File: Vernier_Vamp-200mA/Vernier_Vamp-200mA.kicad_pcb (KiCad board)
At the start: 4 copper layers, 160 x 99.5 mm, 209 parts, among them J1 Conn_01x02, J2 RJ45, J3 Screw_Terminal_01x04, J4 Conn_02x07_Odd_Even, J5 Channel 3, J6 Channel 2, J7 Channel 1, Q1 Si4447ADY, Q2 IRF8707PbF, SW1 DPDT_Hirose, U1 LM4040DBZ-5, U10 OPA2277, U11 OPA2277, U12 OPA2277, U13 OPA2277, U14 OPA2277, U15 OPA1622, U16 OPA1622, U17 OPA1622, U2 LM4040DBZ-5, U3 LM393, U4 TPS7A470x, U5 TPS7A470x, U6 TPS7A33, U7 LTC6655-2.5, U8 DAC8814, U9 OPA2277

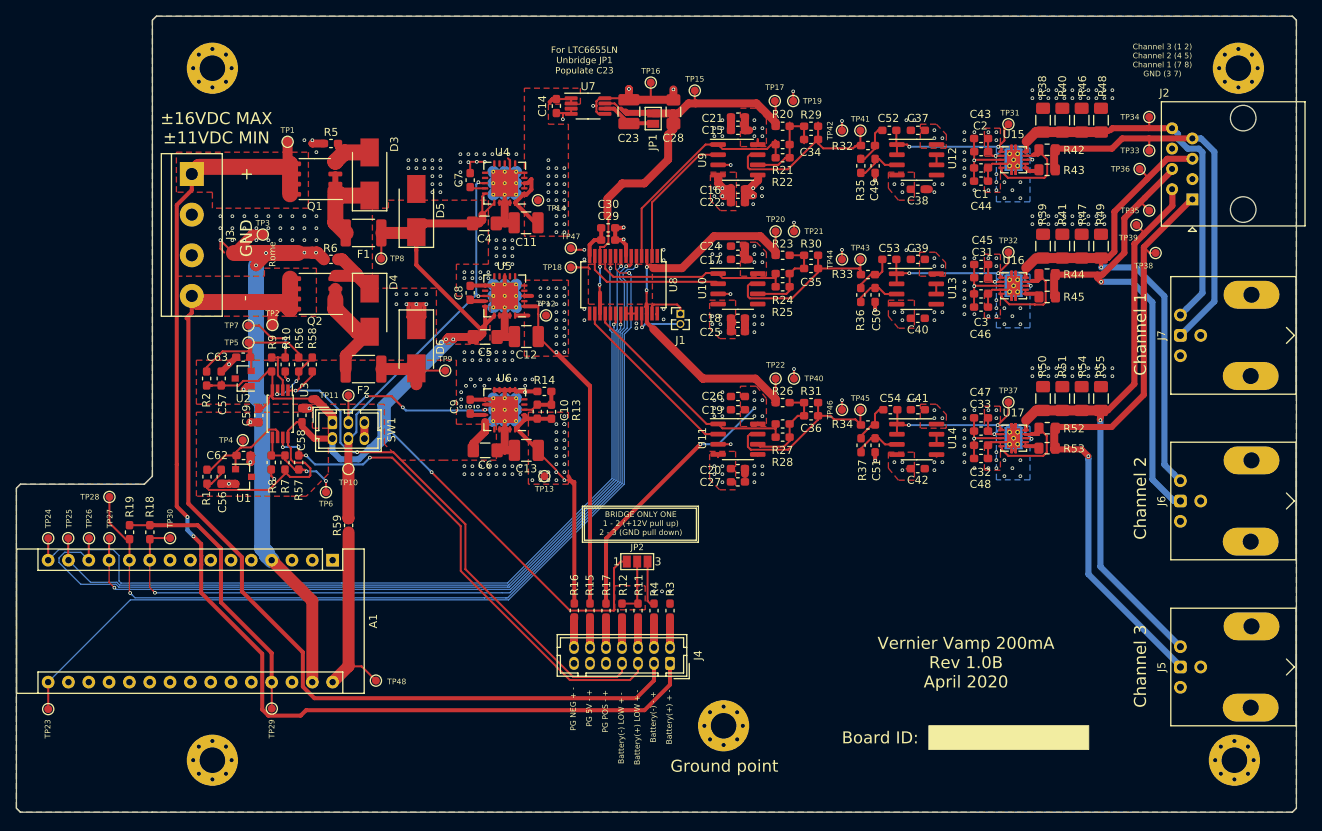
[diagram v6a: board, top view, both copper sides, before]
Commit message: 1.0D Update
LCCD changes
-Addition of trigger for calibration
-PCB optimisation

HCCD changes
-New output stage designed
-Changes from 1.0C applied to HCCD
-New more optimised layout
-New shielding over analog section
-Addition of trigger for calibration

New symbols and footprint creation
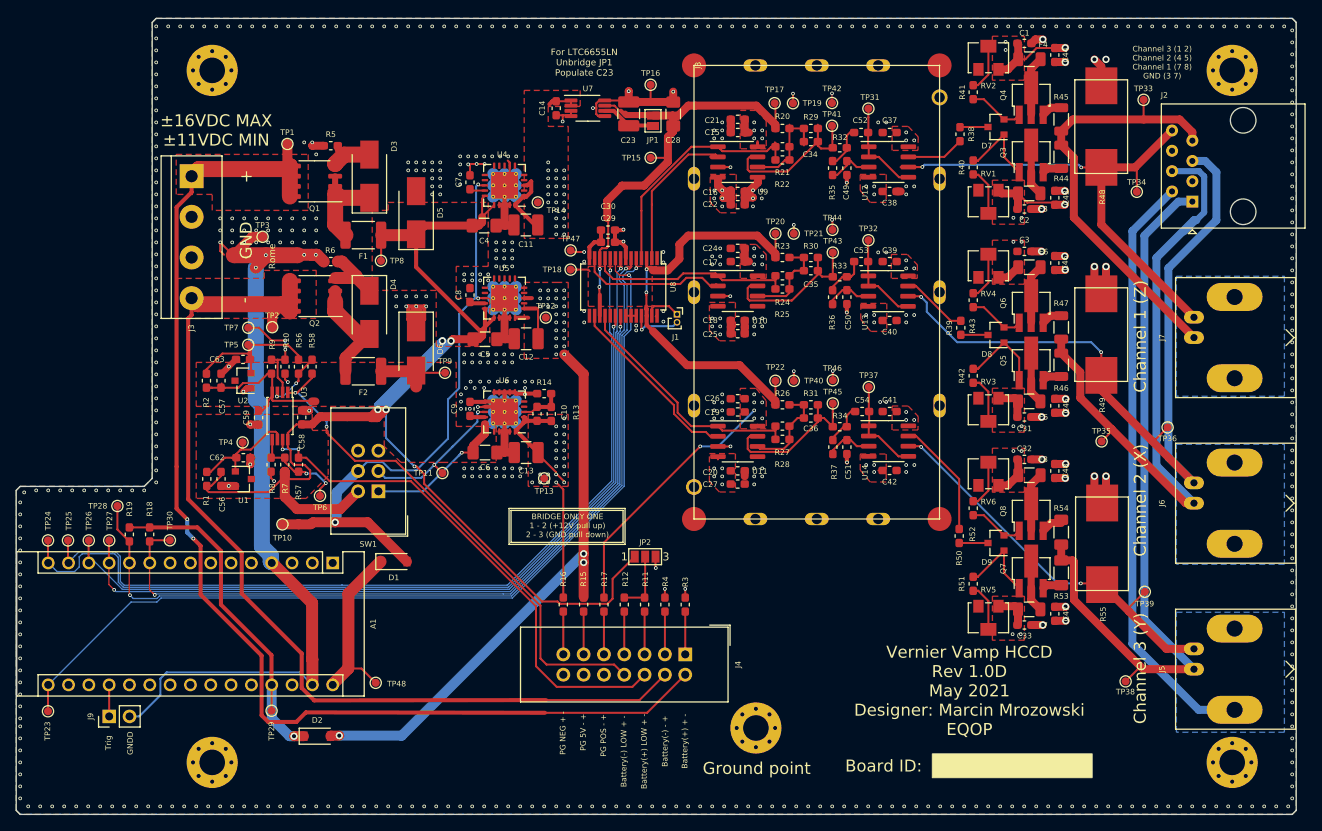
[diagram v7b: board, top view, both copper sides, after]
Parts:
- removed R59: 0R, Resistor_SMD:R_0603_1608Metric_Pad1.05x0.95mm_HandSolder
- removed U15, U16, U17: OPA1622, PVSON-10_ThermalVias-Tented:Texas_S-PVSON-10_ThermalVias-Tented
- added D1: MBR0520LT, Diode_SMD:D_SOD-123, F.Cu at (73.7, 115.9)
- added D2: MBR0520LT, Diode_SMD:D_SOD-123, F.Cu at (64.1, 137.8)
- added D7: BAV99, Package_TO_SOT_SMD:SOT-23, F.Cu at (148.9, 61.6)
- added D8: BAV99, Package_TO_SOT_SMD:SOT-23, F.Cu at (148.9, 87.6)
- added D9: BAV99, Package_TO_SOT_SMD:SOT-23, F.Cu at (148.9, 113.6)
- added F3: 1206L020, Fuse:Fuse_1206_3216Metric, F.Cu at (153.1, 69.9)
- added F4: 1206L020, Fuse:Fuse_1206_3216Metric, F.Cu at (153.1, 53.1)
- added F5: 1206L020, Fuse:Fuse_1206_3216Metric, F.Cu at (153.1, 95.9)
- added F6: 1206L020, Fuse:Fuse_1206_3216Metric, F.Cu at (153.1, 79.1)
- added F7: 1206L020, Fuse:Fuse_1206_3216Metric, F.Cu at (153.1, 121.9)
- added F8: 1206L020, Fuse:Fuse_1206_3216Metric, F.Cu at (153.1, 105.1)
- added J8: RF_Shield_Two_Pieces, MS570-10F:MS570-10S, F.Cu at (111.2, 53.9)
- added J9: Conn_01x02, Connector_PinHeader_2.54mm:PinHeader_1x02_P2.54mm_Vertical, F.Cu at (38.1, 135.3)
- added Q3: 2SC5566, Package_TO_SOT_SMD:SOT-89-3_Handsoldering, F.Cu at (153.3, 65.1)
- added Q4: 2SA2013, Package_TO_SOT_SMD:SOT-89-3_Handsoldering, F.Cu at (153.3, 57.9)
- added Q5: 2SC5566, Package_TO_SOT_SMD:SOT-89-3_Handsoldering, F.Cu at (153.3, 91.1)
- added Q6: 2SA2013, Package_TO_SOT_SMD:SOT-89-3_Handsoldering, F.Cu at (153.3, 83.9)
- added Q7: 2SC5566, Package_TO_SOT_SMD:SOT-89-3_Handsoldering, F.Cu at (153.3, 117.1)
- added Q8: 2SA2013, Package_TO_SOT_SMD:SOT-89-3_Handsoldering, F.Cu at (153.3, 109.9)
- added RV1: 10k, Potentiometer_SMD:Potentiometer_Bourns_3224W_Vertical, F.Cu at (148.0, 71.0)
- added RV2: 10k, Potentiometer_SMD:Potentiometer_Bourns_3224W_Vertical, F.Cu at (148.0, 53.0)
- added RV3: 10k, Potentiometer_SMD:Potentiometer_Bourns_3224W_Vertical, F.Cu at (148.0, 97.0)
- added RV4: 10k, Potentiometer_SMD:Potentiometer_Bourns_3224W_Vertical, F.Cu at (148.0, 79.0)
- added RV5: 10k, Potentiometer_SMD:Potentiometer_Bourns_3224W_Vertical, F.Cu at (148.0, 123.0)
- added RV6: 10k, Potentiometer_SMD:Potentiometer_Bourns_3224W_Vertical, F.Cu at (148.0, 105.0)
- A1: value Arduino_Nano_v3.x -> Arduino_Nano_Every
- J1: footprint Connector_PinHeader_1.27mm:PinHeader_1x02_P1.27mm_Vertical -> Dummy_conn_01x02:PinSocket_1x02_P1.00mm_Vertical_CUSTOM_CYD
- J4: footprint Connector_Hirose:Hirose_DF11-14DP-2DSA_2x07_P2.00mm_Vertical -> Connector_IDC:IDC-Header_2x07_P2.54mm_Vertical
- J5, J6, J7: footprint Connector_Coaxial:BNC_Amphenol_031-6575_Horizontal -> Connector_Coaxial:BNC_Amphenol_B6252HB-NPP3G-50_Horizontal
- R38, R39, R50: value 50R -> 49.9R; footprint Resistor_SMD:R_1206_3216Metric_Pad1.42x1.75mm_HandSolder -> Resistor_SMD:R_0603_1608Metric_Pad1.05x0.95mm_HandSolder
- R40, R41, R51: value 50R -> 3k; footprint Resistor_SMD:R_1206_3216Metric_Pad1.42x1.75mm_HandSolder -> Resistor_SMD:R_0603_1608Metric_Pad1.05x0.95mm_HandSolder
- R42, R43, R52: value 4.7R -> 3k; footprint Resistor_SMD:R_0805_2012Metric_Pad1.15x1.40mm_HandSolder -> Resistor_SMD:R_0603_1608Metric_Pad1.05x0.95mm_HandSolder
- R44, R45: value 4.7R -> 0.47R; footprint Resistor_SMD:R_0805_2012Metric_Pad1.15x1.40mm_HandSolder -> Resistor_SMD:R_1206_3216Metric
- R46, R47: value 50R -> 0.47R; footprint Resistor_SMD:R_1206_3216Metric_Pad1.42x1.75mm_HandSolder -> Resistor_SMD:R_1206_3216Metric
- R48, R49, R55: value 50R -> 13R; footprint Resistor_SMD:R_1206_3216Metric_Pad1.42x1.75mm_HandSolder -> WSM2-13R0-FTR-LF:WSM2 13R0 FTR-LF
- R53: value 4.7R -> 0.47R; footprint Resistor_SMD:R_0805_2012Metric_Pad1.15x1.40mm_HandSolder -> Resistor_SMD:R_1206_3216Metric_Pad1.30x1.75mm_HandSolder
- R54: value 50R -> 0.47R; footprint Resistor_SMD:R_1206_3216Metric_Pad1.42x1.75mm_HandSolder -> Resistor_SMD:R_1206_3216Metric_Pad1.30x1.75mm_HandSolder
- SW1: footprint Connector_Hirose:Hirose_DF11-6DP-2DSA_2x03_P2.00mm_Vertical -> Connector_IDC:IDC-Header_2x03_P2.54mm_Vertical
- moved TP38 53.7 mm to (165.2, 130.9)
- moved TP39 45.9 mm to (167.6, 119.7)
- moved TP36 32.5 mm to (170.4, 99.2)
- moved R46 30.7 mm to (157.1, 91.3), turned to 270 degrees
- moved R42 29.7 mm to (146.1, 92.7), turned to 90 degrees
- moved TP35 29.5 mm to (162.2, 100.9)
- moved C47 26.2 mm to (156.3, 122.5), turned to 90 degrees
- moved R51 25.7 mm to (146.1, 118.7)
- moved C33 24.8 mm to (152.5, 123.8), turned to 0 degrees
- moved R55 23.3 mm to (160.2, 118.8)
- moved R45 22.3 mm to (157.1, 60.6), turned to 270 degrees
- moved R41 22.2 mm to (146.1, 57.2)
- moved R50 20.1 mm to (144.3, 112.7)
- moved C45 19.9 mm to (156.3, 96.5), turned to 90 degrees
- moved R43 18.7 mm to (146.1, 83.2), turned to 90 degrees
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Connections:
- A1 pad 14: /DAC/SDO -> /DAC/SDI
- A1 pad 15: /DAC/SDI -> /DAC/SDO
- A1 pad 19: Net-(A1-Pad19) -> /MCU/Trigger
- J4 pad 1: +BATT -> /Power/Battery_Management/Battery+_C
- J4 pad 10: /Power/Battery_Management/+7.5_PG_A -> GND
- J4 pad 11: GND -> /Power/Battery_Management/+5_PG_A
- J4 pad 12: /Power/Battery_Management/+5_PG_A -> GND
- J4 pad 13: GND -> /Power/Battery_Management/-7.5_PG_C
- J4 pad 14: /Power/Battery_Management/-7.5_PG_C -> GND
- J4 pad 2: /Power/Battery_Management/Battery+_C -> +BATT
- J4 pad 3: -BATT -> /Power/Battery_Management/Battery-_A
- J4 pad 4: /Power/Battery_Management/Battery-_A -> -BATT
- J4 pad 5: /Power/Battery_Management/Battery+_LOW_C -> /Power/Battery_Management/Battery+_LOW_A
- J4 pad 6: /Power/Battery_Management/Battery+_LOW_A -> /Power/Battery_Management/Battery+_LOW_C
- J4 pad 7: /Power/Battery_Management/Battery-_LOW_C -> /Power/Battery_Management/Battery-_LOW_A
- J4 pad 8: /Power/Battery_Management/Battery-_LOW_A -> /Power/Battery_Management/Battery-_LOW_C
- J4 pad 9: GND -> /Power/Battery_Management/+7.5_PG_A
- R38 pad 1: /Channel_Outputs/Coil_Iout_R1 -> Net-(D7-Pad3)
- R38 pad 2: GND -> Net-(R38-Pad2)
- R39 pad 1: /Channel_Outputs/Coil_Iout_R2 -> Net-(D8-Pad3)
- R39 pad 2: GND -> Net-(R39-Pad2)
- R40 pad 1: /Channel_Outputs/Coil_Iout_R1 -> Net-(R40-Pad1)
- R40 pad 2: GND -> Net-(D7-Pad1)
- R41 pad 1: /Channel_Outputs/Coil_Iout_R2 -> Net-(D7-Pad2)
- R41 pad 2: GND -> Net-(R41-Pad2)
- R42 pad 1: /Channel_Outputs/Coil_Iout_1 -> Net-(R42-Pad1)
- R43 pad 1: /Channel_Outputs/Coil_Iout_1 -> Net-(D8-Pad2)
- R44 pad 1: /Channel_Outputs/Coil_Iout_2 -> /Channel_Outputs/Coil_Iout_1
- R45 pad 1: /Channel_Outputs/Coil_Iout_2 -> Net-(Q4-Pad3)
- R45 pad 2: Net-(R45-Pad2) -> /Channel_Outputs/Coil_Iout_1
- R46 pad 1: /Channel_Outputs/Coil_Iout_R1 -> /Channel_Outputs/Coil_Iout_2
- R46 pad 2: GND -> Net-(Q5-Pad3)
- R47 pad 1: /Channel_Outputs/Coil_Iout_R2 -> Net-(Q6-Pad3)
- R47 pad 2: GND -> /Channel_Outputs/Coil_Iout_2
- R50 pad 1: /Channel_Outputs/Coil_Iout_R3 -> Net-(D9-Pad3)
- R50 pad 2: GND -> Net-(R50-Pad2)
- R51 pad 1: /Channel_Outputs/Coil_Iout_R3 -> Net-(R51-Pad1)
- R51 pad 2: GND -> Net-(D9-Pad1)
- R52 pad 1: /Channel_Outputs/Coil_Iout_3 -> Net-(D9-Pad2)
- R54 pad 1: /Channel_Outputs/Coil_Iout_R3 -> Net-(Q8-Pad3)
- R54 pad 2: GND -> /Channel_Outputs/Coil_Iout_3
- TP24 pad 1: /DAC/SDI -> /DAC/SDO
- TP25 pad 1: /DAC/SDO -> /DAC/SDI
- U12 pad 5: GND -> Net-(C52-Pad1)
- U12 pad 6: Net-(U12-Pad6) -> /Channel_Outputs/Coil_Iout_R1
- U12 pad 7: Net-(U12-Pad6) -> Net-(R38-Pad2)
- U13 pad 5: GND -> Net-(C53-Pad1)
- U13 pad 6: Net-(U13-Pad6) -> /Channel_Outputs/Coil_Iout_R2
- U13 pad 7: Net-(U13-Pad6) -> Net-(R39-Pad2)
- U14 pad 5: GND -> Net-(C54-Pad1)
- U14 pad 6: Net-(U14-Pad6) -> /Channel_Outputs/Coil_Iout_R3
- U14 pad 7: Net-(U14-Pad6) -> Net-(R50-Pad2)
- U4 pad 10: Net-(U4-Pad10) -> GND
- U4 pad 11: GND -> Net-(U4-Pad11)
- U4 pad 5: GND -> Net-(U4-Pad5)
- U4 pad 6: Net-(U4-Pad6) -> GND
- U4 pad 8: Net-(U4-Pad8) -> GND
- U5 pad 10: Net-(U5-Pad10) -> GND
- U5 pad 11: GND -> Net-(U5-Pad11)
- U5 pad 8: GND -> Net-(U5-Pad8)
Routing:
- net /Channel_Outputs/Coil_Iout_R3: track 79.5 -> 124.3 mm, vias 1 -> 2
- net +5V: track 57.2 -> 87.1 mm, vias 26 -> 29
- net /Channel_Outputs/Coil_Iout_R2: track 69.7 -> 97.8 mm, vias 1 -> 2
- net GNDD: track 57.1 -> 84.1 mm
- net +12V_batt_post: track 51.1 -> 74.5 mm, vias 2 -> 3
- net /Channel_Outputs/Coil_Iout_R1: track 48.7 -> 64.0 mm, vias 0 -> 2
- net Net-(R50-Pad2): track 0.00 -> 14.8 mm
- net /Channel_Outputs/Coil_Iout_2: track 67.7 -> 82.1 mm, vias 1 -> 0
- net /Channel_Outputs/Coil_Iout_3: track 80.2 -> 94.1 mm, vias 1 -> 0
- net Net-(Q3-Pad3): track 13.9 -> 2.44 mm
- net Net-(D7-Pad1): track 0.00 -> 11.0 mm
- net Net-(D9-Pad1): track 0.00 -> 11.0 mm
- net /Power/+12VDC_bat: track 172.8 -> 182.7 mm, vias 4 -> 5
- net Net-(R52-Pad2): track 15.8 -> 6.00 mm
- net +7V5: track 85.3 -> 75.7 mm, vias 65 -> 59
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- added copper zone on B.Cu, net /Channel_Outputs/Coil_Iout_R1
- added copper zone on B.Cu, net /Channel_Outputs/Coil_Iout_R2
- added copper zone on B.Cu, net /Channel_Outputs/Coil_Iout_R3
- removed copper zone on B.Cu, net -7V5
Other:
- board text added: "Channel 1 (Z)"
- board text added: "Channel 2 (X)"
- board text added: "Channel 3 (Y)"
- board text added: "GNDD"
- board text added: "Trig"
- board text added: "Vernier Vamp HCCD Rev 1.0D May 2021 Designer: Marcin Mrozowski EQOP"
- board text removed: "Vernier Vamp 200mA Rev 1.0B April 2020"
- board text removed: "Vernier Vamp 200mA Rev 1.0B April 2020 Designer: Marcin Mrozowski EQOP"

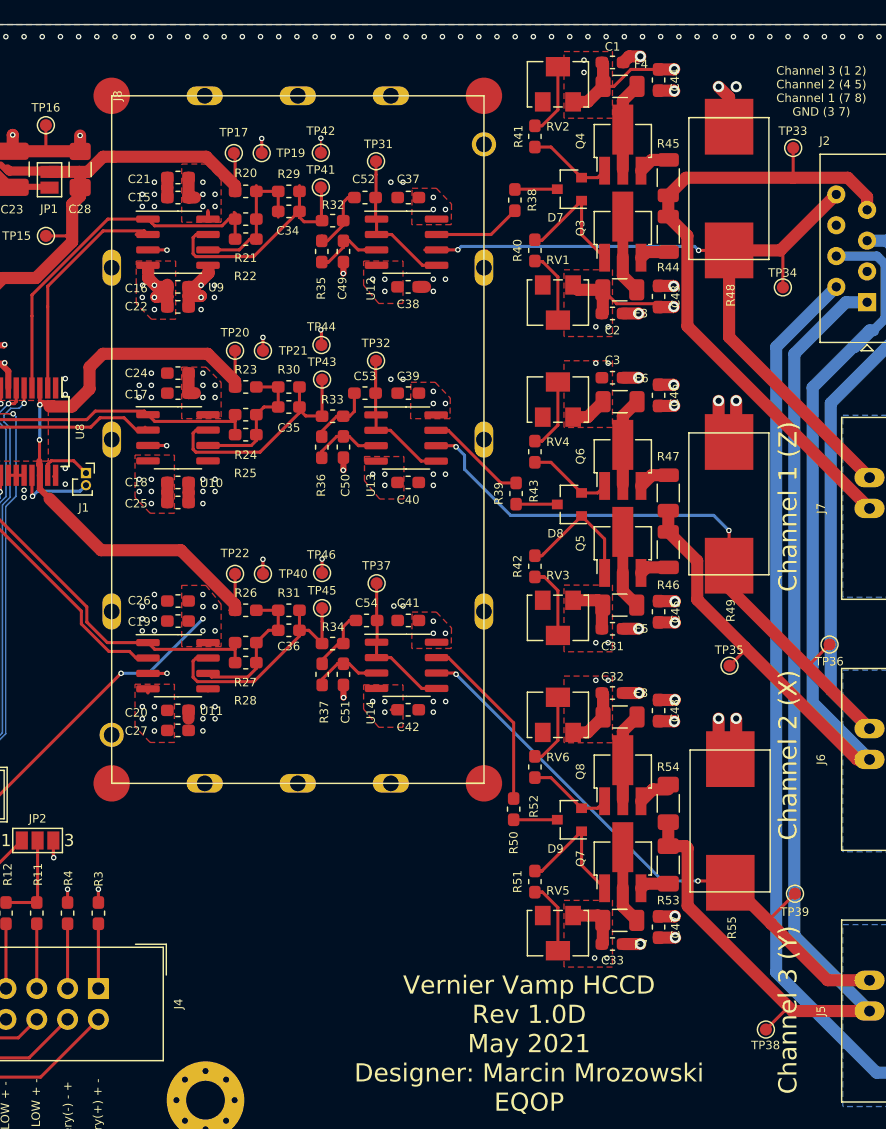
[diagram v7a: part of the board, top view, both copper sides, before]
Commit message: Silkscreen cleanup
-Silkscreen cleanup
-Unconnected items removed
-Addition of calibration software
-Addition of test points for shunt resistor on the bottom layer
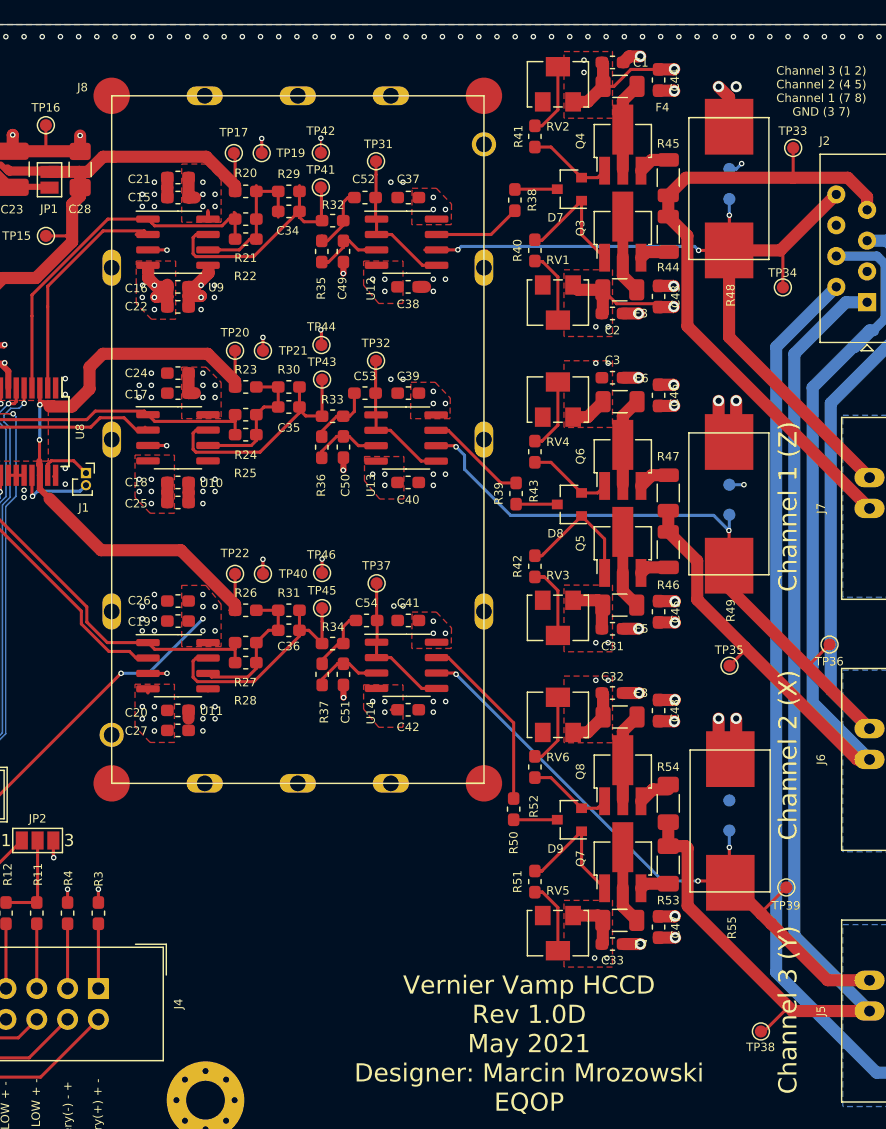
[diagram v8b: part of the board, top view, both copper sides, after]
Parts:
- added TP49: TestPoint_Probe, TestPoint:TestPoint_Pad_D1.0mm, B.Cu at (162.1, 62.4)
- added TP50: TestPoint_Probe, TestPoint:TestPoint_Pad_D1.0mm, B.Cu at (162.1, 59.9)
- added TP51: TestPoint_Probe, TestPoint:TestPoint_Pad_D1.0mm, B.Cu at (162.1, 88.4)
- added TP52: TestPoint_Probe, TestPoint:TestPoint_Pad_D1.0mm, B.Cu at (162.1, 86.0)
- added TP53: TestPoint_Probe, TestPoint:TestPoint_Pad_D1.0mm, B.Cu at (162.1, 114.5)
- added TP54: TestPoint_Probe, TestPoint:TestPoint_Pad_D1.0mm, B.Cu at (162.1, 112.0)
- moved TP39 0.88 mm to (166.8, 119.2)
- moved TP38 0.44 mm to (164.7, 131.1)
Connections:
- A1 pad 1: Net-(A1-Pad1) -> (no net)
- A1 pad 17: Net-(A1-Pad17) -> (no net)
- A1 pad 18: Net-(A1-Pad18) -> (no net)
- A1 pad 2: Net-(A1-Pad2) -> (no net)
- A1 pad 20: Net-(A1-Pad20) -> (no net)
- A1 pad 21: Net-(A1-Pad21) -> (no net)
- A1 pad 22: Net-(A1-Pad22) -> (no net)
- A1 pad 23: Net-(A1-Pad23) -> (no net)
- A1 pad 24: Net-(A1-Pad24) -> (no net)
- A1 pad 25: Net-(A1-Pad25) -> (no net)
- A1 pad 26: Net-(A1-Pad26) -> (no net)
- A1 pad 28: Net-(A1-Pad28) -> (no net)
- A1 pad 3: Net-(A1-Pad3) -> (no net)
- A1 pad 5: Net-(A1-Pad5) -> (no net)
- A1 pad 6: Net-(A1-Pad6) -> (no net)
- A1 pad 7: Net-(A1-Pad7) -> (no net)
- A1 pad 8: Net-(A1-Pad8) -> (no net)
- A1 pad 9: Net-(A1-Pad9) -> (no net)
- RV1 pad 3: Net-(RV1-Pad3) -> (no net)
- RV2 pad 1: Net-(RV2-Pad1) -> (no net)
- RV3 pad 3: Net-(RV3-Pad3) -> (no net)
- RV4 pad 1: Net-(RV4-Pad1) -> (no net)
- RV5 pad 3: Net-(RV5-Pad3) -> (no net)
- RV6 pad 1: Net-(RV6-Pad1) -> (no net)
- U4 pad 11: Net-(U4-Pad11) -> (no net)
- U4 pad 4: Net-(U4-Pad4) -> (no net)
- U4 pad 5: Net-(U4-Pad5) -> (no net)
- U5 pad 11: Net-(U5-Pad11) -> (no net)
- U5 pad 12: Net-(U5-Pad12) -> (no net)
- U5 pad 4: Net-(U5-Pad4) -> (no net)
- U5 pad 5: Net-(U5-Pad5) -> (no net)
- U5 pad 8: Net-(U5-Pad8) -> (no net)
- U5 pad 9: Net-(U5-Pad9) -> (no net)
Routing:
- net /Channel_Outputs/Coil_Iout_R3: track 124.3 -> 128.9 mm, vias 2 -> 3
- net /Channel_Outputs/Coil_Iout_R1: track 64.0 -> 68.2 mm, vias 2 -> 3
- net GND: track 225.7 -> 228.1 mm, vias 577 -> 579
- net /Channel_Outputs/Coil_Iout_R2: track 97.8 -> 99.1 mm
